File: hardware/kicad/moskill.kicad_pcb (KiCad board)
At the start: 2 copper layers, 30 x 100 mm, 90 parts, among them J1 USB-C, Q1 AO3400A, Q2 FS8205A, Q3 2N7002, Q4 2N7002, Q5 2N7002, SW1 Button, T1 EE13 1:20, U1A ESP32-C3-L, U2 AHT20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

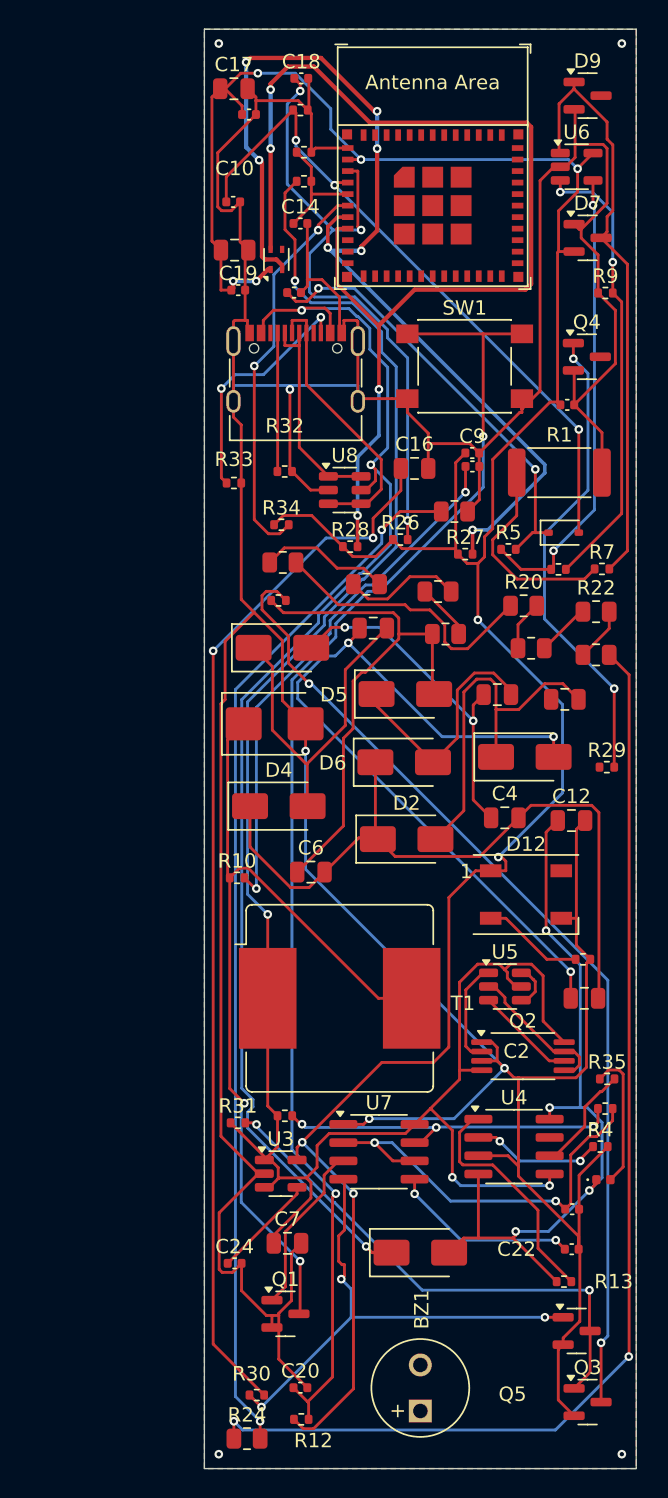
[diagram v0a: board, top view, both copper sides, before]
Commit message: fix(pcb): net class differentiation, power/HV trace widening, fiducials, GND pour
Layout review rework (3.3/10 → improved):
- Net classes: HV (0.25mm/0.4mm clearance), Power (0.3mm/0.25mm),
  Analog (0.2mm/0.3mm), Signal (0.2mm/0.2mm default)
- Trace distribution: 45% signal 0.2mm, 11% HV 0.25mm, 42% power 0.3mm
  (was 93% uniform 0.2mm)
- 3 fiducials (FID1/FID2/FID3) for SMT pick-and-place
- Dual GND copper pour (F.Cu 1455mm² + B.Cu 1273mm²)
- New Gerber export for JLCPCB

Known remaining (8 unconnected, 19 other):
- AHT20 (U2) 3 pins unroutable by FreeRouter (tight 1.5mm DFN keepout)
- USB-C VBUS/CC2 partial connectivity (pad pitch < net class clearance)
- Q2 +BATT gap (TSSOP pitch vs power width)
- 7 clearance: inherent to USB-C/TSSOP pad pitch, needs per-pad exception
- 4 starved thermal, 6 silk overlap (cosmetic)
→ Manual KiCad touch-up recommended for the 8 unconnected
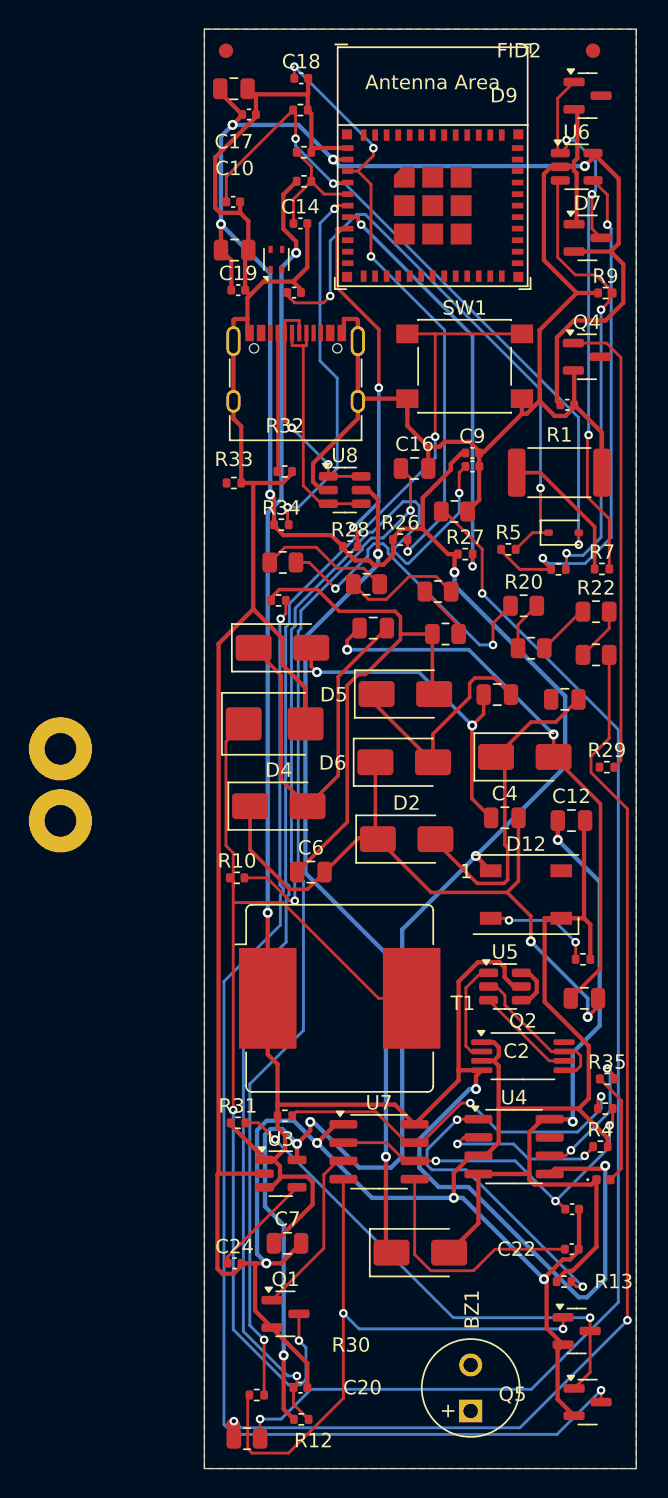
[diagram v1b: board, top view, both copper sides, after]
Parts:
- added FID1: Fiducial, Fiducial_1mm_Mask2mm, F.Cu at (1.50, 1.50)
- added FID2: Fiducial, Fiducial_1mm_Mask2mm, F.Cu at (27.0, 1.50)
- added FID3: Fiducial, Fiducial_1mm_Mask2mm, F.Cu at (2.00, 97.0)
- added H1: M2, MountingHole_2.2mm_M2_Pad, F.Cu at (-10.0, 50.0)
- added H2: M2, MountingHole_2.2mm_M2_Pad, F.Cu at (-10.0, 55.0)
- moved BZ1 3.50 mm to (18.5, 96.0)
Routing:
- net I2C_SCL: track 79.2 -> 24.9 mm, vias 4 -> 2
- net I2C_SDA: track 72.6 -> 29.1 mm, vias 7 -> 2
- net VBUS: track 91.4 -> 58.3 mm, vias 3 -> 2
- net GND: track 356.3 -> 329.0 mm, vias 8 -> 4
- net DISCH_DRN: track 68.3 -> 87.8 mm
- net BLD_8: track 72.7 -> 89.8 mm
- net CC2: track 16.8 -> 0.00 mm, vias 2 -> 0
- net CW_N2: track 54.2 -> 39.2 mm, vias 3 -> 2
- net SNUB_M: track 36.8 -> 50.2 mm
- net +3V3: track 187.8 -> 199.2 mm, vias 9 -> 10
- net FILT_OUT: track 30.3 -> 40.5 mm
- net Q1_DRAIN: track 60.4 -> 70.2 mm
- net +BATT: track 143.0 -> 152.2 mm
- net HV_EN: track 35.1 -> 43.9 mm, vias 3 -> 2
- net HV_RET: track 14.5 -> 9.90 mm
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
